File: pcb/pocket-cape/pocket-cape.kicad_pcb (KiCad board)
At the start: 2 copper layers, 49 x 32.1 mm, 29 parts, among them J1 Sync1, J10 Display, J11 USB1, J2 12..16V, J3 Sync2, J4 Sled, J5 Laser1, J6 PM1, J7 PM2, J8 Laser2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

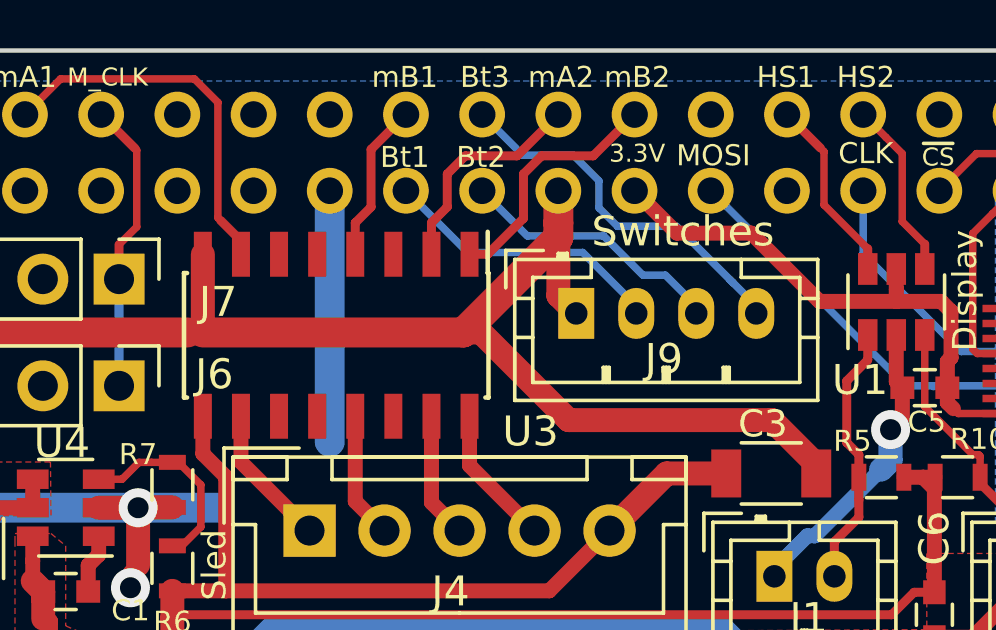
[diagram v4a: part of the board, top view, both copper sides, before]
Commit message: More cooling for ULN2003
o Connect unused pins to a GND copper plane for slightly better
  heat distribution (in any case, we are well within ratings
  of the chip; the sum of all currents is never more than 500mA).
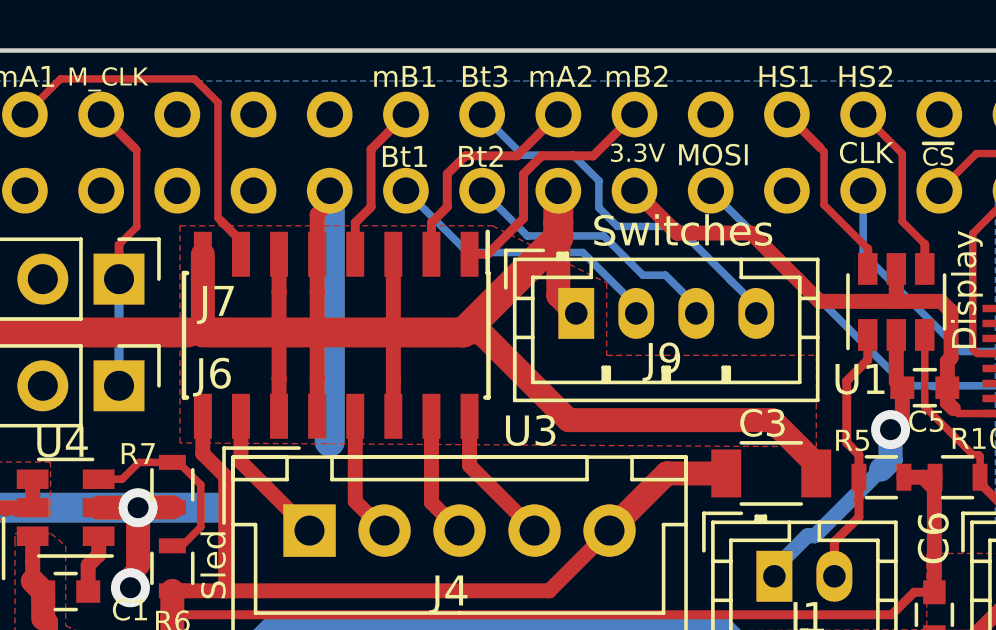
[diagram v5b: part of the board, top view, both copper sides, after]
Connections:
- U3 pad 11: Net-(U3-Pad11) -> GND
- U3 pad 12: Net-(U3-Pad12) -> GND
- U3 pad 14: Net-(U3-Pad14) -> GND
- U3 pad 3: Net-(U3-Pad3) -> GND
- U3 pad 5: Net-(U3-Pad5) -> GND
- U3 pad 6: Net-(U3-Pad6) -> GND
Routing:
- net GND: track 142.9 -> 161.8 mm

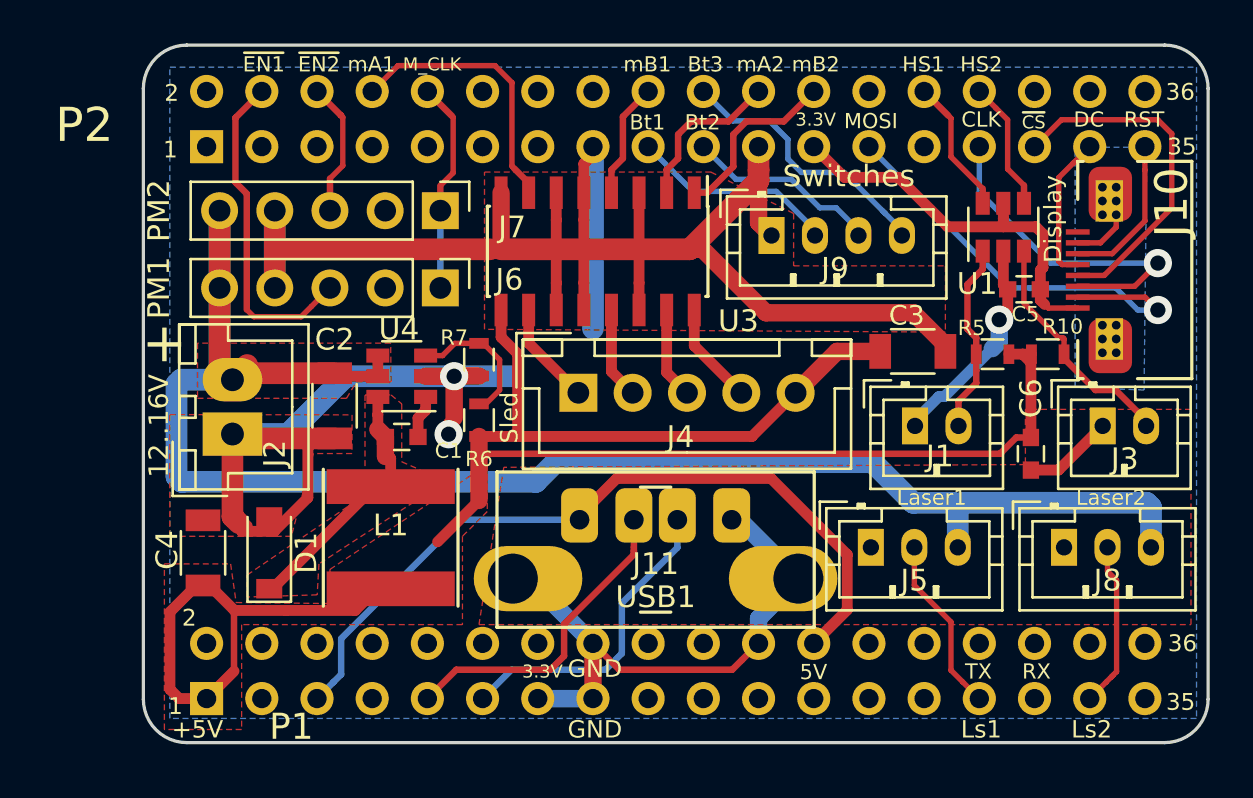
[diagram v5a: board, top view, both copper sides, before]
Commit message: More via stitching between GND planes.
Mostly to heatsink ULN2003, but also in other places to reduce
impedance.
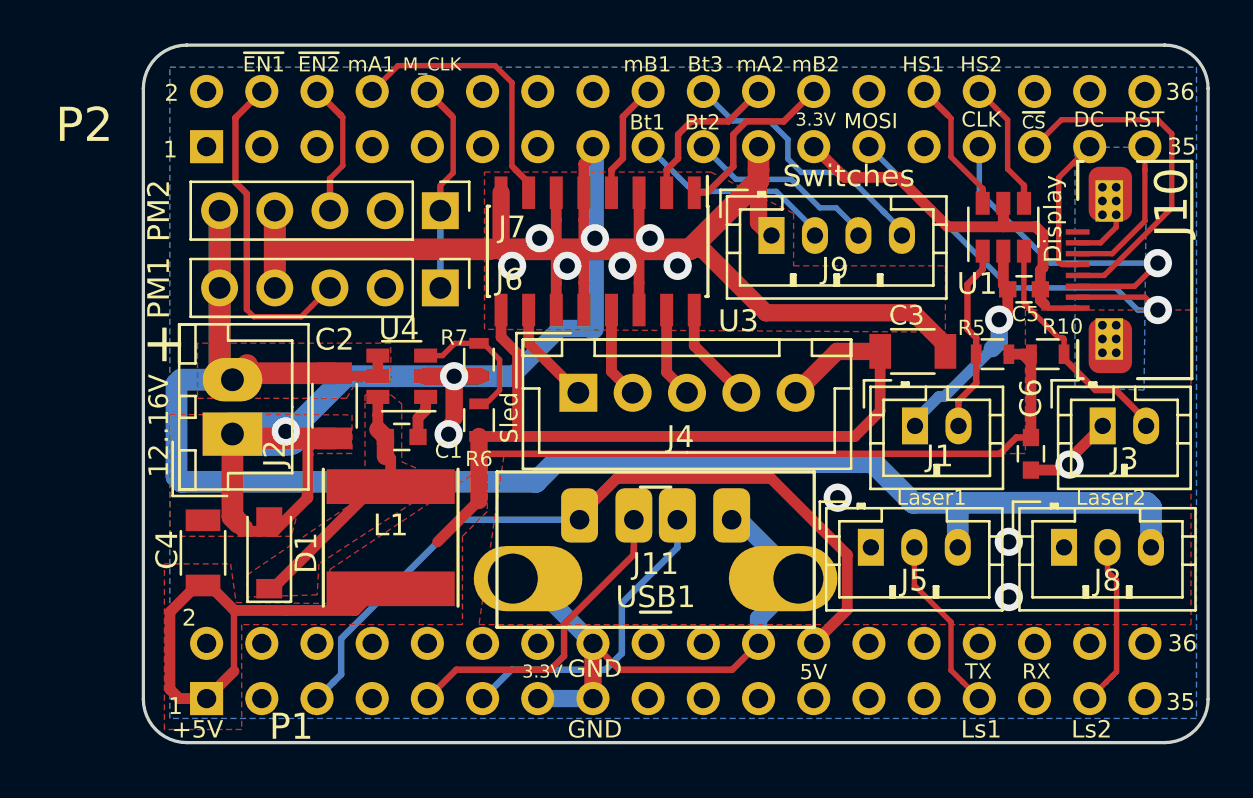
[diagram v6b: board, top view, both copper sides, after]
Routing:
- net VDD_5V: track 86.9 -> 93.1 mm
- net GND: track 161.8 -> 166.4 mm, vias 3 -> 15
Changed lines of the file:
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@@
   (thickness 1.6)
   (drawings 46)
-  (tracks 363)
+  (tracks 378)
   (zones 0)
   (modules 29)
@@
     (effects (font (size 0.77216 0.77216) (thickness 0.097536)) (justify left))
   )
+  (via (at 166.624 108.204) (size 1.3) (drill 0.7) (layers Top Bottom) (net 1))
+  (via (at 155.956 109.728) (size 1.3) (drill 0.7) (layers Top Bottom) (net 1))
+  (via (at 130.556 106.68) (size 1.3) (drill 0.7) (layers Top Bottom) (net 1))
+  (segment (start 143.1671 101.9429) (end 140.97 104.14) (width 0.8) (layer Bottom) (net 1))
+  (segment (start 144.6911 101.9429) (end 143.1671 101.9429) (width 0.8) (layer Bottom) (net 1))
+  (via (at 163.83 114.3) (size 1.3) (drill 0.7) (layers Top Bottom) (net 1))
+  (via (at 163.83 111.76) (size 1.3) (drill 0.7) (layers Top Bottom) (net 1))
+  (via (at 148.59 99.06) (size 1.3) (drill 0.7) (layers Top Bottom) (net 1))
+  (via (at 147.32 97.79) (size 1.3) (drill 0.7) (layers Top Bottom) (net 1))
+  (via (at 146.05 99.06) (size 1.3) (drill 0.7) (layers Top Bottom) (net 1))
+  (via (at 144.78 97.79) (size 1.3) (drill 0.7) (layers Top Bottom) (net 1))
+  (via (at 143.51 99.06) (size 1.3) (drill 0.7) (layers Top Bottom) (net 1))
+  (via (at 142.24 97.79) (size 1.3) (drill 0.7) (layers Top Bottom) (net 1))
+  (via (at 140.97 99.06) (size 1.3) (drill 0.7) (layers Top Bottom) (net 1))
   (segment (start 146.812 101.092) (end 146.812 99.842) (width 0.5) (layer Top) (net 1))
   (segment (start 146.812 99.842) (end 146.812 98.298) (width 0.5) (layer Top) (net 1))
@@
   (segment (start 168.77 97.2775) (end 168.77 96.71) (width 0.25) (layer Top) (net 1))
   (segment (start 144.812 116.3127) (end 144.6911 116.4336) (width 0.8) (layer Top) (net 1))
-  (segment (start 141.224 106.91) (end 152.01 106.91) (width 0.5) (layer Top) (net 2))
+  (segment (start 141.224 106.91) (end 156.742 106.91) (width 0.5) (layer Top) (net 2))
+  (segment (start 156.742 106.91) (end 157.909 105.743) (width 0.5) (layer Top) (net 2))
+  (segment (start 157.909 105.743) (end 157.909 102.997) (width 0.5) (layer Top) (net 2))
   (segment (start 139.446 106.91) (end 141.224 106.91) (width 0.5) (layer Top) (net 2))
   (segment (start 140.462 101.092) (end 140.462 102.342) (width 0.5) (layer Top) (net 2))
@@
   (segment (start 163.421001 107.707999) (end 164.171 106.958) (width 0.3) (layer Top) (net 2))
   (segment (start 164.171 106.958) (end 164.846 106.958) (width 0.3) (layer Top) (net 2))
-  (segment (start 152.01 106.91) (end 154.018 104.902) (width 0.5) (layer Top) (net 2))
   (segment (start 139.446 109.856) (end 137.542 111.76) (width 0.5) (layer Top) (net 2))
   (segment (start 126.9111 118.9736) (end 128.173101 117.711599) (width 0.5) (layer Top) (net 2))
@@
   (segment (start 137.922 104.14) (end 133.318 104.14) (width 1) (layer Bottom) (net 1))
   (segment (start 133.318 104.14) (end 130.658 106.8) (width 1) (layer Bottom) (net 1))
-  (segment (start 130.658 106.8) (end 128.1 106.8) (width 1) (layer Bottom) (net 1))
+  (segment (start 130.658 106.8) (end 128.1 106.8) (width 2) (layer Bottom) (net 1))
   (segment (start 138.303 104.14) (end 138.303 106.045) (width 0.8) (layer Top) (net 1))
   (via (at 138.049 106.807) (size 1.3) (drill 0.7) (layers Top Bottom) (net 1))
@@
     (polygon
       (pts
-        (xy 139.446 115.57) (xy 172.212 115.57) (xy 172.212 105.664) (xy 164.592 105.664) (xy 164.592 108.204)
-        (xy 140.589 108.331)
+        (xy 139.446 115.57) (xy 172.212 115.57) (xy 172.212 101.092) (xy 164.592 101.092) (xy 164.592 107.696)
+        (xy 140.589 107.823)
       )
     )

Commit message: Put a ground-plane near power connector under switcher.
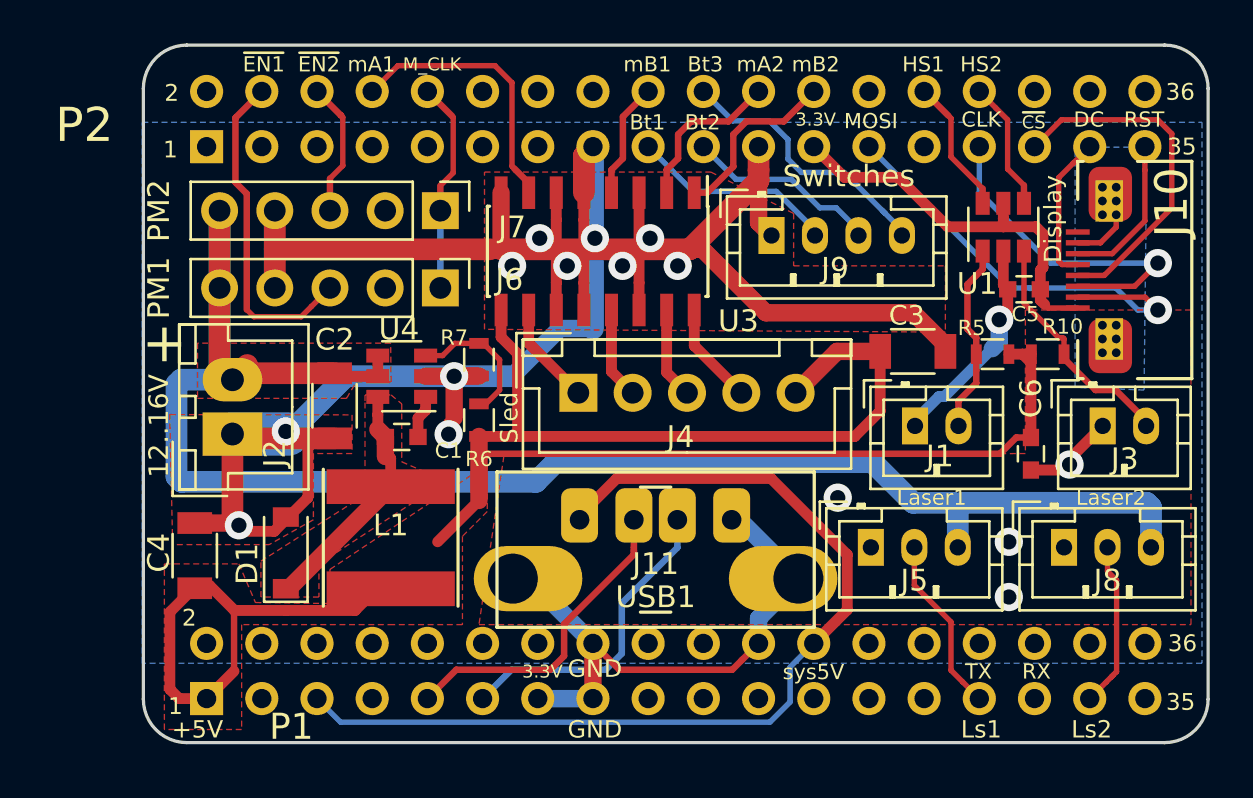
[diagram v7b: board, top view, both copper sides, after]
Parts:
- moved D1 0.76 mm to (130.6, 112.3)
- moved C4 0.40 mm to (126.4, 112.4)
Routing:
- net SYS_VOUT: track 35.8 -> 45.1 mm
- net GND: track 166.4 -> 168.8 mm, vias 15 -> 16
- net /SW: track 13.6 -> 14.5 mm
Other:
- board text added: "sys5V"
- board text removed: "5V"
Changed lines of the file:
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@@
   (thickness 1.6)
   (drawings 46)
-  (tracks 378)
+  (tracks 385)
   (zones 0)
   (modules 29)
@@
 )
 (setup
-  (last_trace_width 0.5)
+  (last_trace_width 0.8)
   (user_trace_width 0.25)
   (user_trace_width 0.3)
@@
   (pad_to_mask_clearance 0.0254)
   (aux_axis_origin 0 0)
-  (visible_elements FFFBEF7F)
+  (visible_elements FFFFEF7F)
   (pcbplotparams
     (layerselection 0x010fc_fffffff9)
@@
   )
   (module Capacitors_SMD:C_1206 (layer Top)
-    (at 126.746 112.268 90)
+    (at 126.365 112.395 90)
     (descr "Capacitor SMD 1206, reflow soldering, AVX (see smccp.pdf)")
     (tags "capacitor 1206")
@@
   )
   (module Diodes_SMD:D_SOD-123 (layer Top)
-    (at 129.794 112.268 90)
+    (at 130.556 112.268 90)
     (descr SOD-123)
     (tags SOD-123)
     (attr smd)
-    (fp_text reference D1 (at 0 1.7 90) (layer F.SilkS)
+    (fp_text reference D1 (at -0.508 -1.778 90) (layer F.SilkS)
       (effects (font (size 1 1) (thickness 0.15)))
     )
@@
     (effects (font (size 0.7 0.7) (thickness 0.12)))
   )
-  (gr_text 5V (at 154.8384 117.7544) (layer F.SilkS)
+  (gr_text sys5V (at 154.8384 117.7544) (layer F.SilkS)
     (effects (font (size 0.7 0.7) (thickness 0.12)))
   )
@@
     (effects (font (size 0.77216 0.77216) (thickness 0.097536)) (justify left))
   )
+  (segment (start 126.365 110.895) (end 128.294 110.895) (width 0.8) (layer Top) (net 1))
+  (segment (start 128.294 110.895) (end 128.397 110.998) (width 0.8) (layer Top) (net 1))
+  (via (at 128.397 110.998) (size 1.3) (drill 0.7) (layers Top Bottom) (net 1))
+  (segment (start 144.6911 93.5736) (end 144.272 93.9927) (width 1) (layer Top) (net 1))
+  (segment (start 144.272 93.9927) (end 144.272 95.692) (width 1) (layer Top) (net 1))
   (via (at 166.624 108.204) (size 1.3) (drill 0.7) (layers Top Bottom) (net 1))
   (via (at 155.956 109.728) (size 1.3) (drill 0.7) (layers Top Bottom) (net 1))
@@
   (segment (start 143.002 95.692) (end 143.002 96.942) (width 0.5) (layer Top) (net 1))
   (segment (start 143.002 96.942) (end 143.002 98.298) (width 0.5) (layer Top) (net 1))
-  (segment (start 144.6911 93.9419) (end 144.272 94.361) (width 0.5) (layer Top) (net 1))
-  (segment (start 144.272 94.361) (end 144.272 95.692) (width 0.5) (layer Top) (net 1))
   (segment (start 144.6911 93.5736) (end 144.6911 93.9419) (width 0.5) (layer Top) (net 1))
   (segment (start 163.7785 100.1395) (end 163.7785 101.1435) (width 0.5) (layer Top) (net 1))
@@
   (segment (start 168.788101 117.736599) (end 168.5417 117.983) (width 0.25) (layer Top) (net 15))
   (segment (start 168.313099 118.211601) (end 167.5511 118.9736) (width 0.25) (layer Top) (net 15))
+  (segment (start 130.556 113.918) (end 130.684 113.918) (width 0.8) (layer Top) (net 16))
+  (segment (start 130.684 113.918) (end 135.382 109.22) (width 0.8) (layer Top) (net 16))
+  (segment (start 134.747 109.22) (end 134.493 109.22) (width 0.8) (layer Top) (net 16))
+  (segment (start 134.874 109.22) (end 134.747 109.22) (width 0.8) (layer Top) (net 16))
+  (segment (start 135.382 109.22) (end 134.874 109.22) (width 0.8) (layer Top) (net 16))
   (segment (start 134.79 105.09) (end 134.79 105.915) (width 0.5) (layer Top) (net 16))
   (segment (start 134.79 105.915) (end 134.79 106.584) (width 0.5) (layer Top) (net 16))
-  (segment (start 129.794 113.918) (end 129.944 113.918) (width 0.5) (layer Top) (net 16))
-  (segment (start 129.944 113.918) (end 134.642 109.22) (width 0.5) (layer Top) (net 16))
   (segment (start 134.642 109.22) (end 135.382 109.22) (width 0.5) (layer Top) (net 16))
   (segment (start 135.14 107.835) (end 135.297 107.835) (width 0.5) (layer Top) (net 16))
@@
   (segment (start 158.142 96.647) (end 158.908 97.413) (width 0.25) (layer Bottom) (net 34))
   (segment (start 158.908 97.413) (end 158.908 97.663) (width 0.25) (layer Bottom) (net 34))
+  (segment (start 131.9911 118.9736) (end 133.078101 120.060601) (width 0.25) (layer Bottom) (net 79))
+  (segment (start 133.078101 120.060601) (end 152.832861 120.060601) (width 0.25) (layer Bottom) (net 79))
+  (segment (start 152.832861 120.060601) (end 153.764099 119.129363) (width 0.25) (layer Bottom) (net 79))
+  (segment (start 153.764099 117.520601) (end 154.089101 117.195599) (width 0.25) (layer Bottom) (net 79))
+  (segment (start 153.764099 119.129363) (end 153.764099 117.520601) (width 0.25) (layer Bottom) (net 79))
+  (segment (start 154.089101 117.195599) (end 154.8511 116.4336) (width 0.25) (layer Bottom) (net 79))
   (segment (start 154.8511 116.4336) (end 156.39401 114.89069) (width 0.5) (layer Top) (net 79))
   (segment (start 156.39401 114.89069) (end 156.39401 112.35041) (width 0.5) (layer Top) (net 79))
@@
   (segment (start 145.786558 108.84399) (end 144.074 110.556548) (width 0.5) (layer Top) (net 79))
   (segment (start 144.074 110.556548) (end 144.074 110.744) (width 0.5) (layer Top) (net 79))
-  (segment (start 144.074 110.744) (end 138.574938 110.744) (width 0.3) (layer Bottom) (net 79))
-  (segment (start 138.574938 110.744) (end 133.103101 116.215837) (width 0.3) (layer Bottom) (net 79))
-  (segment (start 133.103101 116.215837) (end 133.103101 117.861599) (width 0.3) (layer Bottom) (net 79))
-  (segment (start 133.103101 117.861599) (end 132.753099 118.211601) (width 0.3) (layer Bottom) (net 79))
-  (segment (start 132.753099 118.211601) (end 131.9911 118.9736) (width 0.3) (layer Bottom) (net 79))
   (zone (net 1) (net_name GND) (layer Bottom) (hatch edge 0.508)
     (connect_pads (clearance 0.5))
@@
     (polygon
       (pts
-        (xy 172.466 119.888) (xy 125.222 119.888) (xy 125.222 89.916) (xy 172.466 89.916)
+        (xy 172.72 117.348) (xy 123.952 117.348) (xy 123.952 92.456) (xy 172.72 92.456)
       )
     )
@@
     (polygon
       (pts
-        (xy 125.212 105.904) (xy 133.604 105.918) (xy 133.604 107.696) (xy 131.826 107.696) (xy 130.81 111.506)
-        (xy 125.222 111.506)
+        (xy 125.212 105.904) (xy 133.604 105.918) (xy 133.604 107.696) (xy 131.826 107.696) (xy 131.826 110.744)
+        (xy 129.794 111.887) (xy 125.349 111.887)
       )
     )
@@
       (pts
         (xy 134.2 105) (xy 135.4 105) (xy 135.89 105.41) (xy 135.89 108.077) (xy 137.922 108.966)
-        (xy 132.08 112.776) (xy 132 114.2) (xy 128.778 114.3) (xy 128.778 113.284) (xy 134.2 109.6)
+        (xy 132.08 112.776) (xy 132.08 114.3) (xy 129.413 114.3) (xy 129.413 112.649) (xy 134.2 109.6)
         (xy 134.2 105.282)
       )
@@
     (polygon
       (pts
-        (xy 124.968 112.776) (xy 128.016 112.776) (xy 128.27 114.554) (xy 132.6 114.6) (xy 132.588 113.03)
+        (xy 124.968 112.776) (xy 128.397 112.776) (xy 129.159 114.554) (xy 132.6 114.6) (xy 132.588 113.03)
         (xy 139.827 108.204) (xy 139.827 110.363) (xy 138.684 111.506) (xy 138.684 115.57) (xy 135.509 115.57)
         (xy 128.524 115.57) (xy 128.524 120.396) (xy 124.968 120.396)

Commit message: Slowly converting to current kicad.
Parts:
- C5: footprint Capacitors_SMD:C_0603 -> Capacitor_SMD:C_0603_1608Metric
- J5, J8: footprint Connectors_JST:JST_PH_B3B-PH-K_03x2.00mm_Straight -> Connector_JST:JST_PH_B3B-PH-K_1x03_P2.00mm_Vertical
- J6, J7: footprint Pin_Headers:Pin_Header_Straight_1x05_Pitch2.54mm -> Connector_PinHeader_2.54mm:PinHeader_1x05_P2.54mm_Vertical
- REF***: footprint Symbols:OSHW-Symbol_6.7x6mm_SilkScreen -> Symbol:OSHW-Symbol_6.7x6mm_SilkScreen
- U1, U4: footprint TO_SOT_Packages_SMD:SOT-23-6 -> Package_TO_SOT_SMD:SOT-23-6
- U3: footprint Housings_SOIC:SOIC-16_3.9x9.9mm_Pitch1.27mm -> Package_SO:SOIC-16_3.9x9.9mm_P1.27mm
